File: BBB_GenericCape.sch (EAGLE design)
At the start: 3 parts, among them J1 CON_HEADER_2X08SHROUDED, J2 CON_HEADER_2X05-PTH+SHROUDED_A

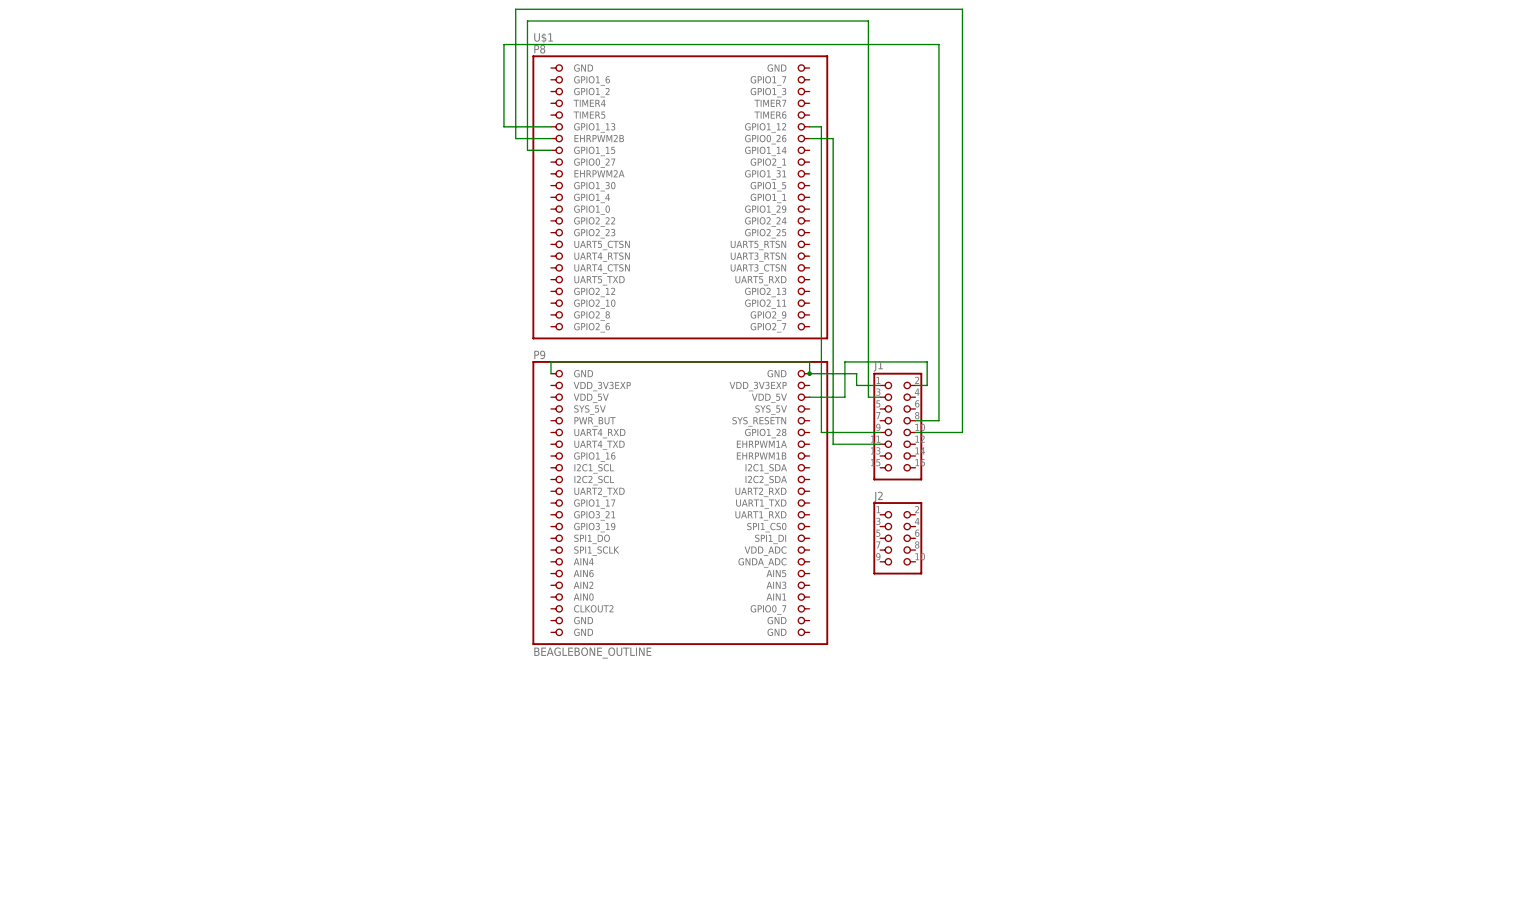
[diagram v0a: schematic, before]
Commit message: fixed bbb cape issue, did something with cable splice
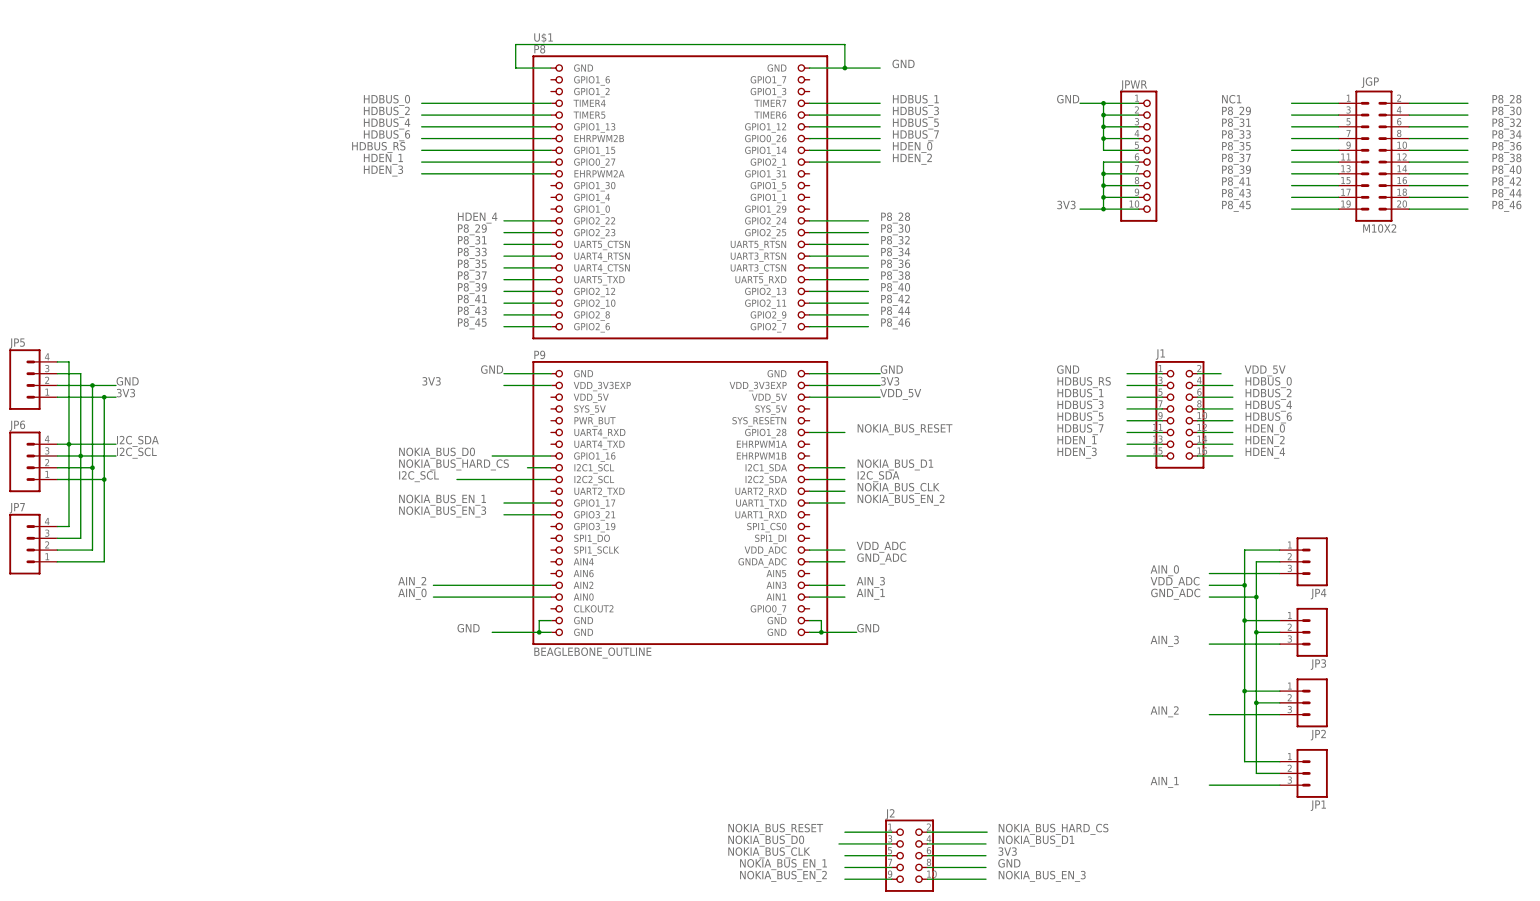
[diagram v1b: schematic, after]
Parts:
- added JGP: M10X2, SparkFun-Connectors:M10X2
- added JP1, JP2, JP3, JP4: (no value), SparkFun-Connectors:M03POLAR
- added JP5, JP6, JP7: (no value), SparkFun-Connectors:M04POLAR
- added JPWR: (no value), pinhead:PINHD-1X10
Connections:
- net N$2 renamed VDD_5V
- net N$3 renamed HDBUS_RS
- net N$4 renamed HDBUS_4
- net N$5 renamed HDBUS_7
- net N$6 renamed HDBUS_6
- net N$7 renamed HDBUS_5
- removed net N$1: J1.1, U$1.GND@1, U$1.GND@2
- new net 3V3: J2.6, JP5.1, JP6.1, JP7.1, JPWR.10, JPWR.6, JPWR.7, JPWR.8, JPWR.9, U$1.VDD_3V3EXP@1, U$1.VDD_3V3EXP@2
- new net AIN_0: JP4.3, U$1.AIN0
- new net AIN_1: JP1.3, U$1.AIN1
- new net AIN_2: JP2.3, U$1.AIN2
- new net AIN_3: JP3.3, U$1.AIN3
- new net GND: J1.1, J2.8, JP5.2, JP6.2, JP7.2, JPWR.1, JPWR.2, JPWR.3, JPWR.4, JPWR.5, U$1.GND@1, U$1.GND@2, U$1.GND@3, U$1.GND@4, U$1.GND@5, U$1.GND@6, U$1.GND@7, U$1.GND@8
- new net GND_ADC: JP1.2, JP2.2, JP3.2, JP4.2, U$1.GNDA_ADC
- new net HDBUS_0: J1.4, U$1.TIMER4
- new net HDBUS_1: J1.5, U$1.TIMER7
- new net HDBUS_2: J1.6, U$1.TIMER5
- new net HDBUS_3: J1.7, U$1.TIMER6
- new net HDEN_0: J1.12, U$1.GPIO1_14
- new net HDEN_1: J1.13, U$1.GPIO0_27
- new net HDEN_2: J1.14, U$1.GPIO2_1
- new net HDEN_3: J1.15, U$1.EHRPWM2A
- new net HDEN_4: J1.16, U$1.GPIO2_22
- new net I2C_SCL: JP5.3, JP6.3, JP7.3, U$1.I2C2_SCL
- new net I2C_SDA: JP5.4, JP6.4, JP7.4, U$1.I2C2_SDA
- new net NC1: JGP.1
- new net NOKIA_BUS_CLK: J2.5, U$1.UART2_RXD
- new net NOKIA_BUS_D0: J2.3, U$1.GPIO1_16
- new net NOKIA_BUS_D1: J2.4, U$1.I2C1_SDA
- new net NOKIA_BUS_EN_1: J2.7, U$1.GPIO1_17
- new net NOKIA_BUS_EN_2: J2.9, U$1.UART1_TXD
- new net NOKIA_BUS_EN_3: J2.10, U$1.GPIO3_21
- new net NOKIA_BUS_HARD_CS: J2.2, U$1.I2C1_SCL
- new net NOKIA_BUS_RESET: J2.1, U$1.GPIO1_28
- new net P8_28: JGP.2, U$1.GPIO2_24
- new net P8_29: JGP.3, U$1.GPIO2_23
- new net P8_30: JGP.4, U$1.GPIO2_25
- new net P8_31: JGP.5, U$1.UART5_CTSN
- new net P8_32: JGP.6, U$1.UART5_RTSN
- new net P8_33: JGP.7, U$1.UART4_RTSN
- new net P8_34: JGP.8, U$1.UART3_RTSN
- new net P8_35: JGP.9, U$1.UART4_CTSN
- new net P8_36: JGP.10, U$1.UART3_CTSN
- new net P8_37: JGP.11, U$1.UART5_TXD
- new net P8_38: JGP.12, U$1.UART5_RXD
- new net P8_39: JGP.13, U$1.GPIO2_12
- new net P8_40: JGP.14, U$1.GPIO2_13
- new net P8_41: JGP.15, U$1.GPIO2_10
- new net P8_42: JGP.16, U$1.GPIO2_11
- new net P8_43: JGP.17, U$1.GPIO2_8
- new net P8_44: JGP.18, U$1.GPIO2_9
- new net P8_45: JGP.19, U$1.GPIO2_6
- new net P8_46: JGP.20, U$1.GPIO2_7
- new net VDD_ADC: JP1.1, JP2.1, JP3.1, JP4.1, U$1.VDD_ADC
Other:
- moved on the sheet: J1, J2
